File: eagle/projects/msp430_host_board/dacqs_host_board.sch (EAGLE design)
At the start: 91 parts, among them J1 MOL-KK-4P-V, J10 MOL-KK-3P-V, J13 JST-PH-2TH-RA, J14 USB_MICROB_RECPT, J16 MOL-KK-2-RA, J17 CLM-112-02-L-D, J18 MOL-KK-2-V, J2 MOL-KK-4P-V, J3 MOL-KK-4P-V, J4 MOL-KK-4P-V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

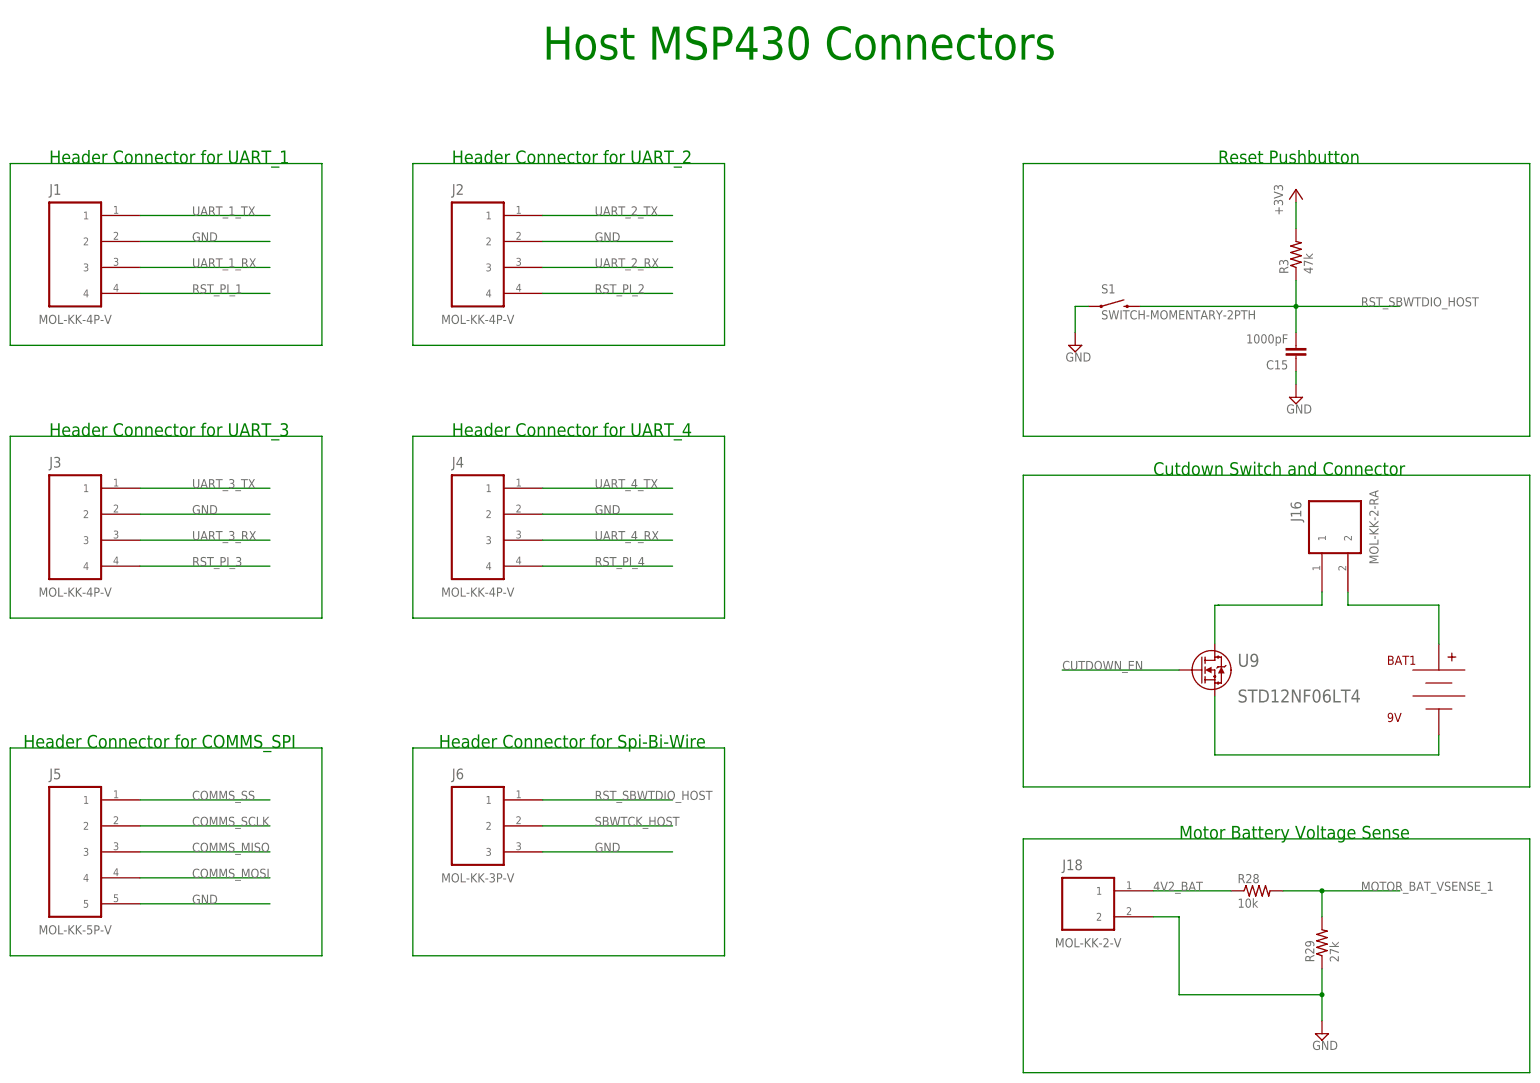
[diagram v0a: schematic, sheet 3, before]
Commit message: Added SL connectors to host library and swapped SL for KK
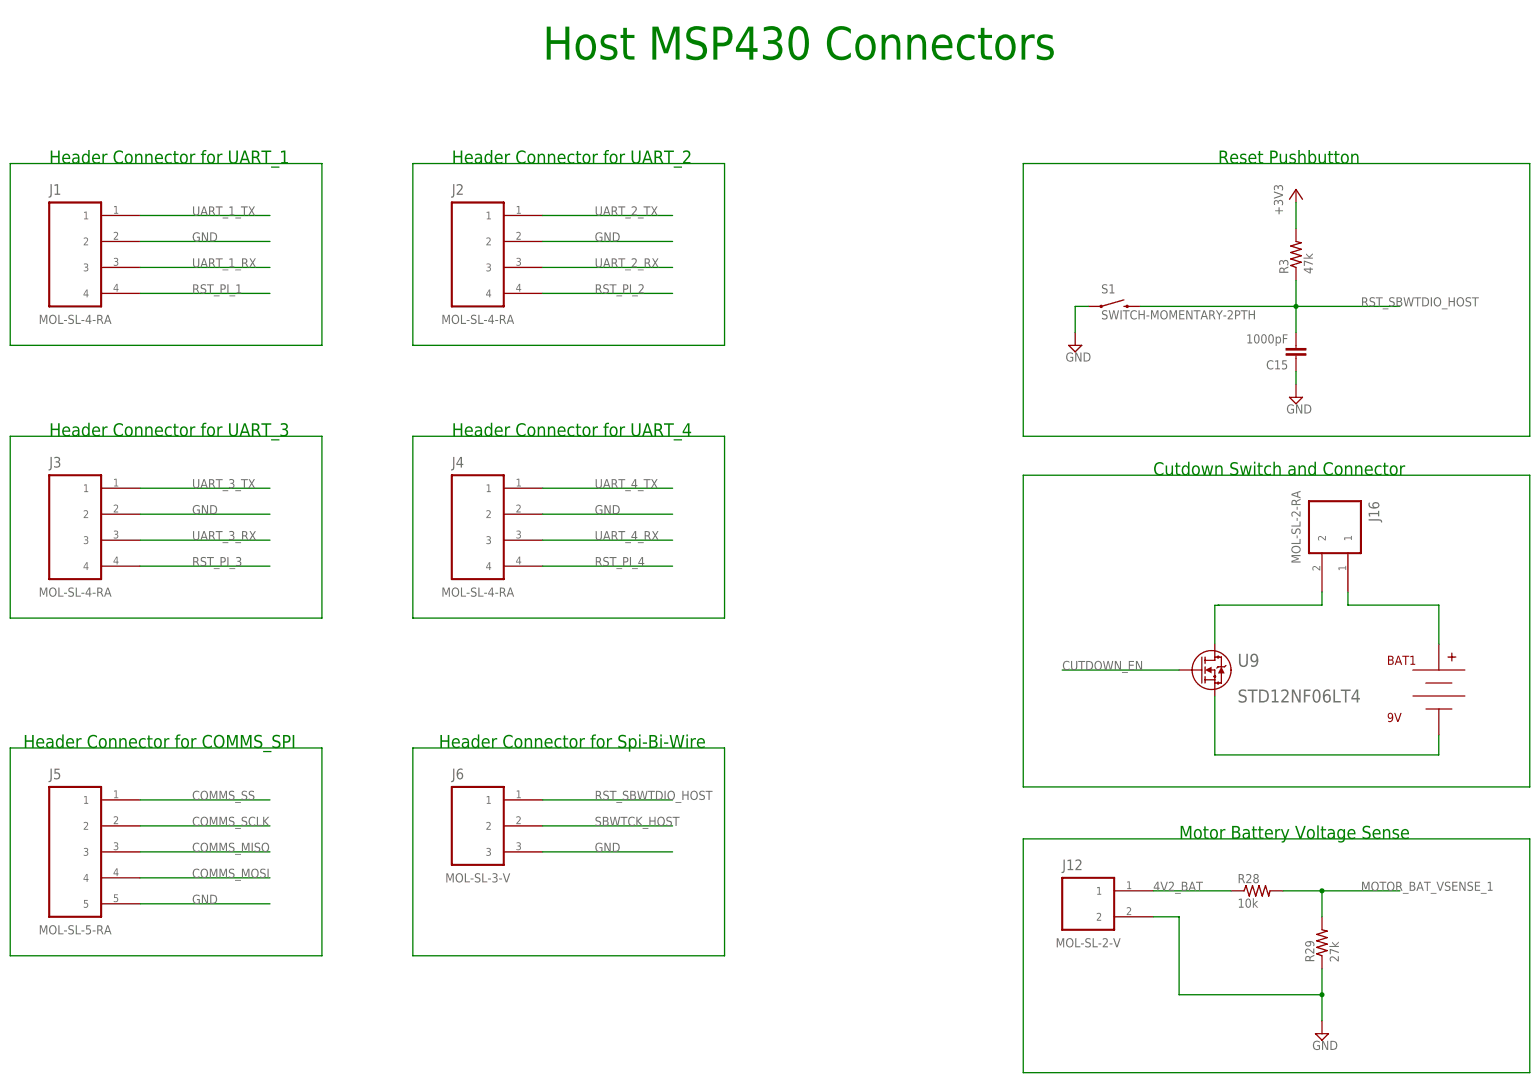
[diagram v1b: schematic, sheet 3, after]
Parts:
- removed J18: MOL-KK-2-V, daqcs_host:MOLKK_2PIN2V_2V
- added J12: MOL-SL-2-V, daqcs_host:MOLSL_2PIN_SL2V_V
- J1, J2, J3, J4: value MOL-KK-4P-V -> MOL-SL-4-RA; device daqcs_host:MOLKK_4PIN_4V_V -> daqcs_host:MOLSL_4PIN_SL4RA_RA
- J10, J6, J9: value MOL-KK-3P-V -> MOL-SL-3-V; device daqcs_host:MOLKK_3PIN_3V_V -> daqcs_host:MOLSL_3PIN_SL3V_V
- J16: value MOL-KK-2-RA -> MOL-SL-2-RA; device daqcs_host:MOLKK_2PIN_2RA_2RA -> daqcs_host:MOLSL_2PIN_SL2RA_RA
- J5: value MOL-KK-5P-V -> MOL-SL-5-RA; device daqcs_host:MOLKK_5PIN_5V_V -> daqcs_host:MOLSL_5PIN_SL4RA_RA
- J7: value MOL-KK-5P-V -> MOL-SL-5-V; device daqcs_host:MOLKK_5PIN_5RA_RA -> daqcs_host:MOLSL_5PIN_SL4V_V
- J8: value MOL-KK-3P-RA -> MOL-SL-3-RA; device daqcs_host:MOLKK_3PIN_3RA_RA -> daqcs_host:MOLSL_3PIN_SL3RA_RA
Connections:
- net 4V2_BAT: now also J12.1; no longer J18.1
- net GND: now also J12.2; no longer J18.2
- net N$39: now also J16.2; no longer J16.1
- net N$40: now also J16.1; no longer J16.2

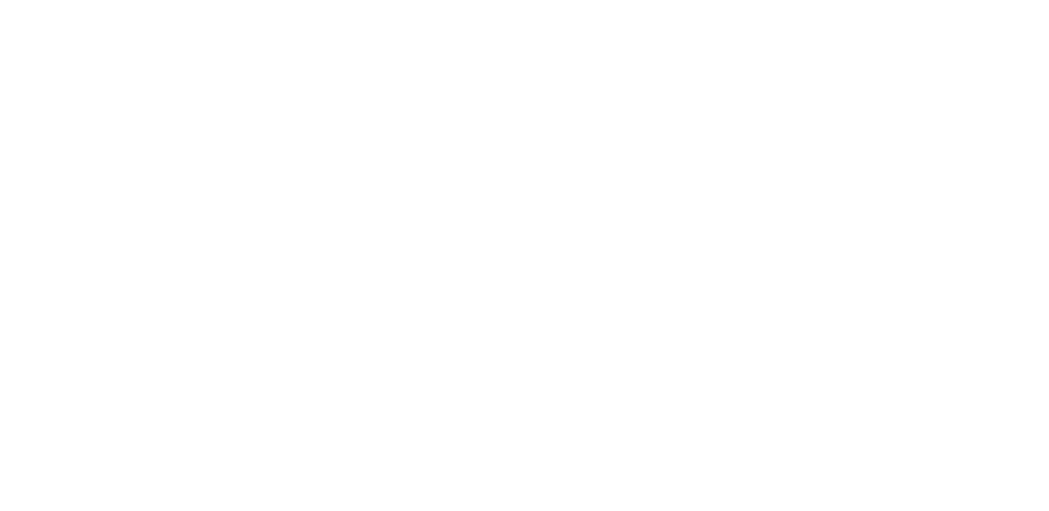
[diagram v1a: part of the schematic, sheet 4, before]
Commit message: Added mounting holes to DAQCS Host Board
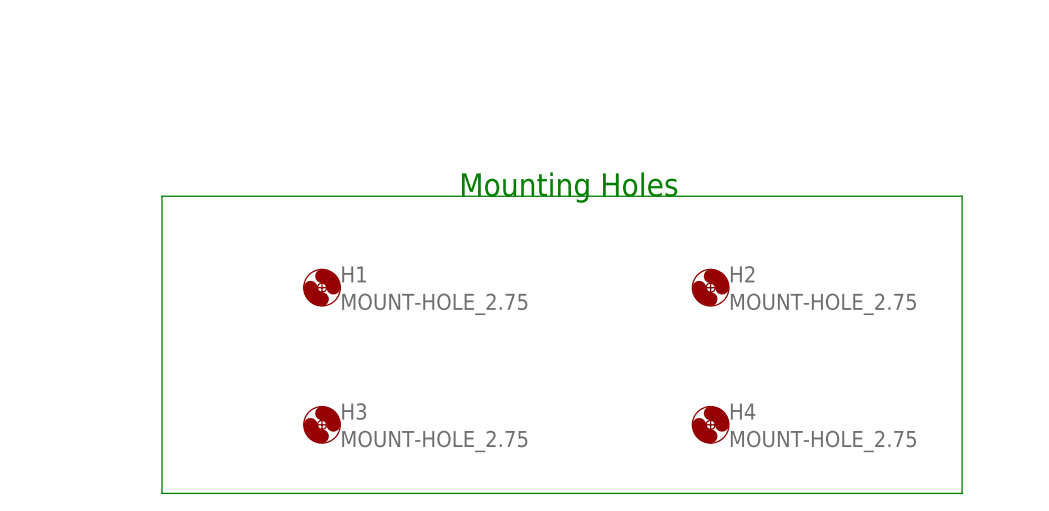
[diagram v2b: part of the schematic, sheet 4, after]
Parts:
- added H1, H2, H3, H4: MOUNT-HOLE_2.75, daqcs_host:MOUNT-HOLE_2.75
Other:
- note added: "Mounting Holes"
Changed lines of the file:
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@@
 <setting verticaltext="up"/>
 </settings>
-<grid distance="0.1" unitdist="inch" unit="inch" style="lines" multiple="1" display="no" altdistance="0.01" altunitdist="inch" altunit="inch"/>
+<grid distance="0.1" unitdist="inch" unit="inch" style="lines" multiple="1" display="yes" altdistance="0.01" altunitdist="inch" altunit="inch"/>
 <layers>
 <layer number="1" name="Top" color="4" fill="1" visible="no" active="no"/>
@@
 <part name="J9" library="daqcs_host" deviceset="MOLSL_3PIN" device="_V" technology="_SL3V" value="MOL-SL-3-V"/>
 <part name="J10" library="daqcs_host" deviceset="MOLSL_3PIN" device="_V" technology="_SL3V" value="MOL-SL-3-V"/>
+<part name="H1" library="daqcs_host" deviceset="MOUNT-HOLE" device="_2.75"/>
+<part name="H2" library="daqcs_host" deviceset="MOUNT-HOLE" device="_2.75"/>
+<part name="H3" library="daqcs_host" deviceset="MOUNT-HOLE" device="_2.75"/>
+<part name="H4" library="daqcs_host" deviceset="MOUNT-HOLE" device="_2.75"/>
 </parts>
 <sheets>
@@
 <text x="228.6" y="215.9" size="2.54" layer="91">Reset Pushbutton </text>
 <text x="101.6" y="231.14" size="6.4516" layer="91">Motor MSP430 Connectors</text>
+<text x="228.6" y="81.28" size="2.54" layer="91">Mounting Holes</text>
 </plain>
 <instances>
@@
 <instance part="J9" gate="G$1" x="55.88" y="66.04"/>
 <instance part="J10" gate="G$1" x="218.44" y="127"/>
+<instance part="H1" gate="G$1" x="213.36" y="71.12"/>
+<instance part="H2" gate="G$1" x="256.54" y="71.12"/>
+<instance part="H3" gate="G$1" x="213.36" y="55.88"/>
+<instance part="H4" gate="G$1" x="256.54" y="55.88"/>
 </instances>
 <busses>
@@
 </segment>
 </net>
+<net name="N$55" class="0">
+<segment>
+<wire x1="195.58" y1="81.28" x2="284.48" y2="81.28" width="0.1524" layer="91"/>
+<wire x1="284.48" y1="81.28" x2="284.48" y2="48.26" width="0.1524" layer="91"/>
+<wire x1="284.48" y1="48.26" x2="195.58" y2="48.26" width="0.1524" layer="91"/>
+<wire x1="195.58" y1="48.26" x2="195.58" y2="81.28" width="0.1524" layer="91"/>
+</segment>
+</net>

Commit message: Added battery sense circuits
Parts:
- added R30, R31, R32, R33, R34, R35: 10k, daqcs_host:RES_10R0_0603
- added R36, R37, R38, R39, R40, R41: 27k, daqcs_host:RES_27R0_0603
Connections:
- new net VBAT_CELL_1: R35.1
- new net VBAT_CELL_2: R30.2
- new net VBAT_CELL_3: R31.2
- new net VBAT_CELL_4: R32.2
- new net VBAT_CELL_5: R33.2
- new net VBAT_CELL_6: R34.2
- new net VBAT_MOD_CELL_1: R35.2, R36.1
- new net VBAT_MOD_CELL_2: R30.1, R37.1
- new net VBAT_MOD_CELL_3: R31.1, R38.1
- new net VBAT_MOD_CELL_4: R32.1, R39.1
- new net VBAT_MOD_CELL_5: R33.1, R40.1
- new net VBAT_MOD_CELL_6: R34.1, R41.1
- net GND: now also R36.2, R37.2, R38.2, R39.2, R40.2, R41.2
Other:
- note added: "Reaction Wheel Battery Voltage Sense"
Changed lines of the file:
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@@
 <part name="H3" library="daqcs_host" deviceset="MOUNT-HOLE" device="_2.75"/>
 <part name="H4" library="daqcs_host" deviceset="MOUNT-HOLE" device="_2.75"/>
+<part name="FRAME7" library="frames" deviceset="A3L-LOC" device=""/>
+<part name="R30" library="daqcs_host" deviceset="RES" device="_0603" technology="_10R0" value="10k"/>
+<part name="R31" library="daqcs_host" deviceset="RES" device="_0603" technology="_10R0" value="10k"/>
+<part name="R32" library="daqcs_host" deviceset="RES" device="_0603" technology="_10R0" value="10k"/>
+<part name="R33" library="daqcs_host" deviceset="RES" device="_0603" technology="_10R0" value="10k"/>
+<part name="R34" library="daqcs_host" deviceset="RES" device="_0603" technology="_10R0" value="10k"/>
+<part name="R35" library="daqcs_host" deviceset="RES" device="_0603" technology="_10R0" value="10k"/>
+<part name="R36" library="daqcs_host" deviceset="RES" device="_0603" technology="_27R0" value="27k"/>
+<part name="R37" library="daqcs_host" deviceset="RES" device="_0603" technology="_27R0" value="27k"/>
+<part name="R38" library="daqcs_host" deviceset="RES" device="_0603" technology="_27R0" value="27k"/>
+<part name="R39" library="daqcs_host" deviceset="RES" device="_0603" technology="_27R0" value="27k"/>
+<part name="R40" library="daqcs_host" deviceset="RES" device="_0603" technology="_27R0" value="27k"/>
+<part name="R41" library="daqcs_host" deviceset="RES" device="_0603" technology="_27R0" value="27k"/>
+<part name="SUPPLY31" library="supply2" deviceset="GND" device=""/>
+<part name="SUPPLY33" library="supply2" deviceset="GND" device=""/>
+<part name="SUPPLY34" library="supply2" deviceset="GND" device=""/>
+<part name="SUPPLY35" library="supply2" deviceset="GND" device=""/>
+<part name="SUPPLY36" library="supply2" deviceset="GND" device=""/>
+<part name="SUPPLY37" library="supply2" deviceset="GND" device=""/>
 </parts>
 <sheets>
@@
 </segment>
 </net>
+</nets>
+</sheet>
+<sheet>
+<plain>
+<text x="96.52" y="213.36" size="2.54" layer="91">Reaction Wheel Battery Voltage Sense</text>
+</plain>
+<instances>
+<instance part="FRAME7" gate="G$1" x="0" y="0"/>
+<instance part="R30" gate="G$1" x="132.08" y="187.96" rot="R90"/>
+<instance part="R31" gate="G$1" x="182.88" y="187.96" rot="R90"/>
+<instance part="R32" gate="G$1" x="76.2" y="121.92" rot="R90"/>
+<instance part="R33" gate="G$1" x="132.08" y="121.92" rot="R90"/>
+<instance part="R34" gate="G$1" x="182.88" y="119.38" rot="R90"/>
+<instance part="R35" gate="G$1" x="76.2" y="187.96" rot="R270"/>
+<instance part="R36" gate="G$1" x="76.2" y="167.64" rot="R270"/>
+<instance part="R37" gate="G$1" x="132.08" y="167.64" rot="R270"/>
+<instance part="R38" gate="G$1" x="182.88" y="165.1" rot="R270"/>
+<instance part="R39" gate="G$1" x="76.2" y="96.52" rot="R270"/>
+<instance part="R40" gate="G$1" x="132.08" y="96.52" rot="R270"/>
+<instance part="R41" gate="G$1" x="182.88" y="96.52" rot="R270"/>
+<instance part="SUPPLY31" gate="GND" x="76.2" y="154.94"/>
+<instance part="SUPPLY33" gate="GND" x="132.08" y="154.94"/>
+<instance part="SUPPLY34" gate="GND" x="182.88" y="152.4"/>
+<instance part="SUPPLY35" gate="GND" x="182.88" y="83.82"/>
+<instance part="SUPPLY36" gate="GND" x="132.08" y="83.82"/>
+<instance part="SUPPLY37" gate="GND" x="76.2" y="83.82"/>
+</instances>
+<busses>
+</busses>
+<nets>
+<net name="VBAT_CELL_1" class="0">
+<segment>
+<pinref part="R35" gate="G$1" pin="1"/>
+<wire x1="76.2" y1="193.04" x2="76.2" y2="200.66" width="0.1524" layer="91"/>
+<wire x1="76.2" y1="200.66" x2="99.06" y2="200.66" width="0.1524" layer="91"/>
+<label x="81.28" y="200.66" size="1.778" layer="95"/>
+</segment>
+</net>
+<net name="VBAT_MOD_CELL_1" class="0">
+<segment>
+<pinref part="R35" gate="G$1" pin="2"/>
+<pinref part="R36" gate="G$1" pin="1"/>
+<wire x1="76.2" y1="182.88" x2="76.2" y2="177.8" width="0.1524" layer="91"/>
+<wire x1="76.2" y1="177.8" x2="76.2" y2="172.72" width="0.1524" layer="91"/>
+<wire x1="76.2" y1="177.8" x2="50.8" y2="177.8" width="0.1524" layer="91"/>
+<junction x="76.2" y="177.8"/>
+<label x="50.8" y="177.8" size="1.778" layer="95"/>
+</segment>
+</net>
+<net name="VBAT_CELL_2" class="0">
+<segment>
+<pinref part="R30" gate="G$1" pin="2"/>
+<wire x1="132.08" y1="193.04" x2="132.08" y2="200.66" width="0.1524" layer="91"/>
+<wire x1="132.08" y1="200.66" x2="152.4" y2="200.66" width="0.1524" layer="91"/>
+<label x="137.16" y="200.66" size="1.778" layer="95"/>
+</segment>
+</net>
+<net name="VBAT_MOD_CELL_2" class="0">
+<segment>
+<pinref part="R30" gate="G$1" pin="1"/>
+<pinref part="R37" gate="G$1" pin="1"/>
+<wire x1="132.08" y1="182.88" x2="132.08" y2="177.8" width="0.1524" layer="91"/>
+<wire x1="132.08" y1="177.8" x2="132.08" y2="172.72" width="0.1524" layer="91"/>
+<wire x1="132.08" y1="177.8" x2="106.68" y2="177.8" width="0.1524" layer="91"/>
+<junction x="132.08" y="177.8"/>
+<label x="106.68" y="177.8" size="1.778" layer="95"/>
+</segment>
+</net>
+<net name="VBAT_MOD_CELL_3" class="0">
+<segment>
+<pinref part="R31" gate="G$1" pin="1"/>
+<pinref part="R38" gate="G$1" pin="1"/>
+<wire x1="182.88" y1="182.88" x2="182.88" y2="177.8" width="0.1524" layer="91"/>
+<wire x1="182.88" y1="177.8" x2="182.88" y2="170.18" width="0.1524" layer="91"/>
+<wire x1="182.88" y1="177.8" x2="157.48" y2="177.8" width="0.1524" layer="91"/>
+<junction x="182.88" y="177.8"/>
+<label x="157.48" y="177.8" size="1.778" layer="95"/>
+</segment>
+</net>
+<net name="VBAT_CELL_3" class="0">
+<segment>
+<pinref part="R31" gate="G$1" pin="2"/>
+<wire x1="182.88" y1="193.04" x2="182.88" y2="200.66" width="0.1524" layer="91"/>
+<wire x1="182.88" y1="200.66" x2="205.74" y2="200.66" width="0.1524" layer="91"/>
+<label x="187.96" y="200.66" size="1.778" layer="95"/>
+</segment>
+</net>
+<net name="VBAT_CELL_4" class="0">
+<segment>
+<pinref part="R32" gate="G$1" pin="2"/>
+<wire x1="76.2" y1="127" x2="76.2" y2="134.62" width="0.1524" layer="91"/>
+<wire x1="76.2" y1="134.62" x2="99.06" y2="134.62" width="0.1524" layer="91"/>
+<label x="83.82" y="134.62" size="1.778" layer="95"/>
+</segment>
+</net>
+<net name="VBAT_MOD_CELL_4" class="0">
+<segment>
+<pinref part="R32" gate="G$1" pin="1"/>
+<pinref part="R39" gate="G$1" pin="1"/>
+<wire x1="76.2" y1="116.84" x2="76.2" y2="109.22" width="0.1524" layer="91"/>
+<wire x1="76.2" y1="109.22" x2="76.2" y2="101.6" width="0.1524" layer="91"/>
+<wire x1="76.2" y1="109.22" x2="50.8" y2="109.22" width="0.1524" layer="91"/>
+<junction x="76.2" y="109.22"/>
+<label x="50.8" y="109.22" size="1.778" layer="95"/>
+</segment>
+</net>
+<net name="VBAT_CELL_5" class="0">
+<segment>
+<pinref part="R33" gate="G$1" pin="2"/>
+<wire x1="132.08" y1="127" x2="132.08" y2="132.08" width="0.1524" layer="91"/>
+<wire x1="132.08" y1="132.08" x2="152.4" y2="132.08" width="0.1524" layer="91"/>
+<label x="137.16" y="132.08" size="1.778" layer="95"/>
+</segment>
+</net>
+<net name="VBAT_MOD_CELL_5" class="0">
+<segment>
+<pinref part="R33" gate="G$1" pin="1"/>
+<pinref part="R40" gate="G$1" pin="1"/>
+<wire x1="132.08" y1="116.84" x2="132.08" y2="109.22" width="0.1524" layer="91"/>
+<wire x1="132.08" y1="109.22" x2="132.08" y2="101.6" width="0.1524" layer="91"/>
+<wire x1="132.08" y1="109.22" x2="106.68" y2="109.22" width="0.1524" layer="91"/>
+<junction x="132.08" y="109.22"/>
+<label x="106.68" y="109.22" size="1.778" layer="95"/>
+</segment>
+</net>
+<net name="VBAT_CELL_6" class="0">
+<segment>
+<pinref part="R34" gate="G$1" pin="2"/>
+<wire x1="182.88" y1="124.46" x2="182.88" y2="132.08" width="0.1524" layer="91"/>
+<wire x1="182.88" y1="132.08" x2="205.74" y2="132.08" width="0.1524" layer="91"/>
+<label x="187.96" y="132.08" size="1.778" layer="95"/>
+</segment>
+</net>
+<net name="VBAT_MOD_CELL_6" class="0">
+<segment>
+<pinref part="R34" gate="G$1" pin="1"/>
+<pinref part="R41" gate="G$1" pin="1"/>
+<wire x1="182.88" y1="114.3" x2="182.88" y2="106.68" width="0.1524" layer="91"/>
+<wire x1="182.88" y1="106.68" x2="182.88" y2="101.6" width="0.1524" layer="91"/>
+<wire x1="182.88" y1="106.68" x2="154.94" y2="106.68" width="0.1524" layer="91"/>
+<junction x="182.88" y="106.68"/>
+<label x="154.94" y="106.68" size="1.778" layer="95"/>
+</segment>
+</net>
+<net name="GND" class="0">
+<segment>
+<pinref part="R36" gate="G$1" pin="2"/>
+<wire x1="76.2" y1="162.56" x2="76.2" y2="157.48" width="0.1524" layer="91"/>
+<pinref part="SUPPLY31" gate="GND" pin="GND"/>
+</segment>
+<segment>
+<pinref part="R37" gate="G$1" pin="2"/>
+<wire x1="132.08" y1="162.56" x2="132.08" y2="157.48" width="0.1524" layer="91"/>
+<pinref part="SUPPLY33" gate="GND" pin="GND"/>
+</segment>
+<segment>
+<pinref part="R38" gate="G$1" pin="2"/>
+<wire x1="182.88" y1="160.02" x2="182.88" y2="154.94" width="0.1524" layer="91"/>
+<pinref part="SUPPLY34" gate="GND" pin="GND"/>
+</segment>
+<segment>
+<pinref part="R41" gate="G$1" pin="2"/>
+<wire x1="182.88" y1="91.44" x2="182.88" y2="86.36" width="0.1524" layer="91"/>
+<pinref part="SUPPLY35" gate="GND" pin="GND"/>
+</segment>
+<segment>
+<pinref part="R40" gate="G$1" pin="2"/>
+<wire x1="132.08" y1="91.44" x2="132.08" y2="86.36" width="0.1524" layer="91"/>
+<pinref part="SUPPLY36" gate="GND" pin="GND"/>
+</segment>
+<segment>
+<pinref part="R39" gate="G$1" pin="2"/>
+<wire x1="76.2" y1="91.44" x2="76.2" y2="86.36" width="0.1524" layer="91"/>
+<pinref part="SUPPLY37" gate="GND" pin="GND"/>
+</segment>
+</net>
+<net name="N$56" class="0">
+<segment>
+<wire x1="35.56" y1="213.36" x2="218.44" y2="213.36" width="0.1524" layer="91"/>
+<wire x1="218.44" y1="213.36" x2="218.44" y2="76.2" width="0.1524" layer="91"/>
+<wire x1="218.44" y1="76.2" x2="35.56" y2="76.2" width="0.1524" layer="91"/>
+<wire x1="35.56" y1="76.2" x2="35.56" y2="213.36" width="0.1524" layer="91"/>
+</segment>
+</net>
